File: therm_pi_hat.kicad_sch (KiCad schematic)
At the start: 50 parts

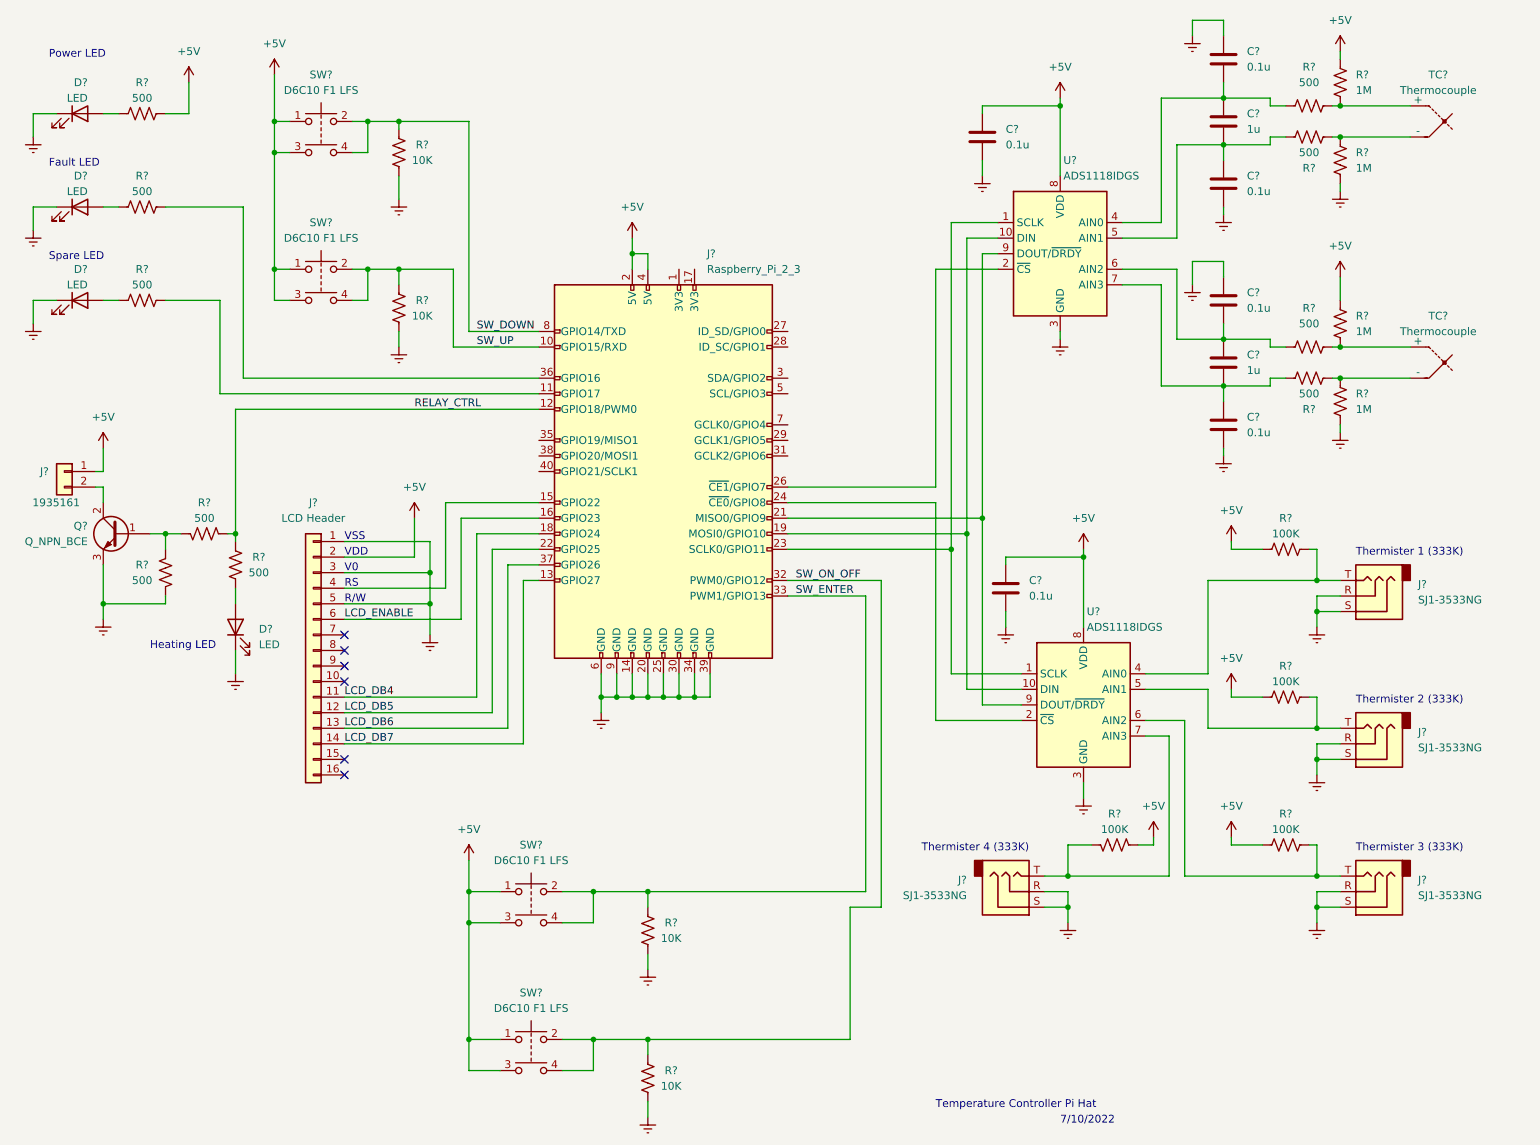
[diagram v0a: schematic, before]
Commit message: added polygon to board cut layer of pcb
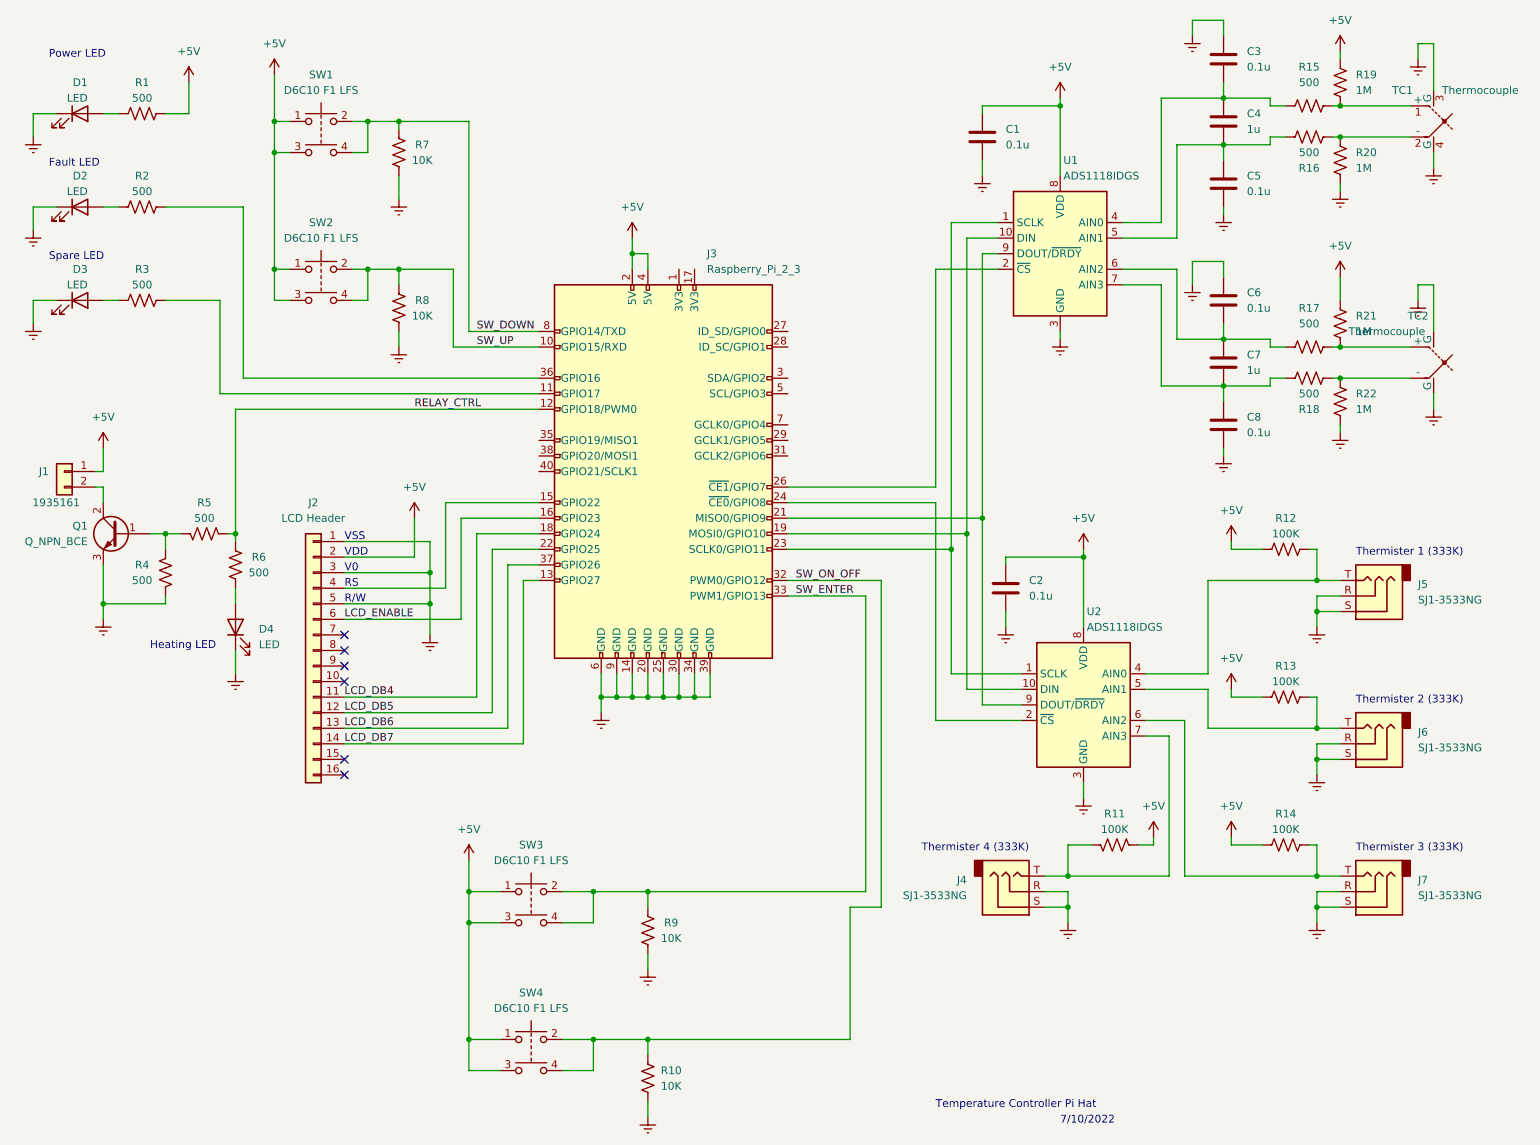
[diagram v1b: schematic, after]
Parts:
- removed TC?: Thermocouple, symbol Device:Thermocouple
- added TC1: Thermocouple, Library:thermocouple, symbol Device:Thermocouple
- TC2: renamed from TC?; footprint (none) -> Library:thermocouple
- gave numbers to parts that had none: 48
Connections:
- net GNDREF: now also TC2.3 (G), TC2.4 (G), TC1.3 (G), TC1.4 (G)
- net at R15.2, R19.2: now also TC1.1 (+)
- net at R16.1, R20.1: now also TC1.2 (-)
